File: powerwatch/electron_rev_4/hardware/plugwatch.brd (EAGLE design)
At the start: 55.7 x 95.2 mm, 128 parts, among them J1 CON_MICRO_SDDM3AT-SF-PEJM5, U1 BGA725L6-ALT, U10 SIP32510, U12 SIP32510, U13 AB1815-T3, U16 MAX6746, U2 SAFFB1G56KB0F0A, U20 DS2401P+, U3 IRM-03-5V, U4 MAX-M8, U5 OPA369, U6 LIS2DW12, U8 OPA369, U9 SIP32510, X1 ABS07-32.768KHZ-7-T

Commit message: renumbered eagle parts
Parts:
- removed C19: 0.1uF, passives:0402_CAP
- removed C26: 4.7uF, passives:0402_CAP
- removed D11: (no value), passives:SOD323
- removed J4: (no value), SparkFun-Connectors:JST-2-SMD
- removed RF, RF1: 4.99k 1%, passives:0402_RES
- removed RI1, RI3: 953k 1%, passives:1206_RES_HIGH_CLEARANCE
- removed RI2, RI4: 953k 1%, passives:0402_RES
- removed U16: MAX6746, chips:SOT-23-8
- removed U20: DS2401P+, DS2401P+:21-0382
- added C10: 1uF, passives:0402_CAP
- added C16: 100uF, passives:1210_CAP
- added D2: (no value), passives:SOD323
- added J2: (no value), SparkFun-Connectors:JST-2-SMD
- added R20: 34k, passives:0402_RES
- added R37, R38, R39, R40: 1M, passives:0402_RES
- added U11: SIP32510, chips:TSOT23-6
- added U14: (no value), microphones:SPH0465
- added V1: S14K385, varistor:S14K385
- C1: value 1uF -> 47pF
- C11: value 10nF -> 1uF
- C12: value 10nF -> 4.7uF
- C15: value 100nF -> 100uF; device passives:0402_CAP -> passives:1210_CAP
- C17: value 100uF -> 2000uF; device passives:1210_CAP -> rcl:E5-13
- C2: value 2000uF -> 10nF; device rcl:E5-13 -> passives:0402_CAP
- C3: value 47pF -> 10nF
- C4: value 1uF -> 0.1uF
- C7: value 100uF -> 100nF; device passives:1210_CAP -> passives:0402_CAP
- D1: value BLUE -> (none); device leds:LED-0603 -> passives:SOD323
- D4, D5, D6, D7: value 3.3V -> (none)
- D9: value (none) -> BLUE; device passives:SOD323 -> leds:LED-0603
- R1: value 10k -> 66.5
- R10: value 10k -> 5k
- R11: value 68 -> 10k
- R15, R16, R17, R18, R19: value 100k -> 10k
- R2: value 10k -> 68
- R21: value 750k -> 100k; device passives:1206_RES_HIGH_CLEARANCE -> passives:0402_RES
- R22, R23, R25: value 1M 1% -> 100k
- R24: value 835k -> 100k
- R26: value 68 -> 100k
- R28: value 1M 1% -> 750k; device passives:0402_RES -> passives:1206_RES_HIGH_CLEARANCE
- R29: value 5K -> 750k; device passives:0402_RES -> passives:1206_RES_HIGH_CLEARANCE
- R32: value 1.5k -> 835k
- R33: value 1.5k -> 953k
- R34: value 10k -> 953k
- R35: value 66.5 -> 953k; device passives:0402_RES -> passives:1206_RES_HIGH_CLEARANCE
- R36: value 34k -> 953k; device passives:0402_RES -> passives:1206_RES_HIGH_CLEARANCE
- R4: value 1k -> 68
- R5: value 100k -> 1k
- R6: value 10k -> 1.5k
- R7: value S14K385 -> 1.5k; device varistor:S14K385 -> passives:0402_RES
- R8: value 750k -> 4.99k; device passives:1206_RES_HIGH_CLEARANCE -> passives:0402_RES
- R9: value 10k -> 4.99k
- U1: value BGA725L6-ALT -> AB1815-T3; device Particle:LNA-TSLP-6-2-ALT -> chips:QFN-16-3MM
- U10, U9: value SIP32510 -> OPA369; device chips:TSOT23-6 -> powerfilm:SC70-5
- U13: value AB1815-T3 -> SIP32510; device chips:QFN-16-3MM -> chips:TSOT23-6
- U2: value SAFFB1G56KB0F0A -> BGA725L6-ALT; device Particle:QCS5I -> Particle:LNA-TSLP-6-2-ALT
- U3: value IRM-03-5V -> DS2401P+; device powerwatch:IRM-03 -> DS2401P+:21-0382
- U4: value MAX-M8 -> SAFFB1G56KB0F0A; device u-blox:MAX-M8 -> Particle:QCS5I
- U5: value OPA369 -> IRM-03-5V; device powerfilm:SC70-5 -> powerwatch:IRM-03
- U7: value (none) -> MAX-M8; device microphones:SPH0465 -> u-blox:MAX-M8
- U8: value OPA369 -> MAX6746; device powerfilm:SC70-5 -> chips:SOT-23-8
- moved R36 71.4 mm to (6.86, 15.4)
- moved U3 70.2 mm to (3.05, 80.5), turned to 270 degrees
- moved R25 66.2 mm to (7.37, 76.2), turned to 180 degrees
- moved R29 64.8 mm to (6.86, 19.9), turned to 180 degrees
- moved R34 62.0 mm to (2.79, 14.2)
- moved U8 59.2 mm to (32.6, 63.2), turned to 90 degrees
- moved R9 59.1 mm to (2.79, 13.3), turned to 180 degrees
- moved R35 57.2 mm to (6.99, 29.7)
- moved R21 56.3 mm to (31.2, 70.7), turned to 90 degrees
- moved U10 56.2 mm to (3.17, 11.9), turned to 180 degrees
- moved U9 55.5 mm to (3.43, 33.0), turned to 90 degrees
- moved R22 52.2 mm to (28.4, 76.8), turned to 0 degrees
- moved U13 44.1 mm to (49.8, 63.6), turned to 0 degrees
- moved R23 44.0 mm to (39.9, 55.8)
- moved D9 44.0 mm to (37.3, 50.0), turned to 90 degrees
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- renumbered A2 to A1, B2 to B1, C100 to C5, C101 to C6, C24 to C9, C27 to C14, C29 to C8, D10 to D3, L4 to L2, L5 to L3
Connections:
- net !EXTERNAL_RST: now also R19.2, TP26.TESTPOINT, U8.7; no longer R1.2, TP17.TESTPOINT, U16.7
- net !GPS_RESET: now also TP10.TESTPOINT, U7.9; no longer TP23.TESTPOINT, U4.9
- net !RTC_CS: now also R18.2, TP23.TESTPOINT, U1.12; no longer R6.2, TP11.TESTPOINT, U13.12
- net !RTC_INT1: now also R17.2, TP24.TESTPOINT, U1.11; no longer R34.2, TP15.TESTPOINT, U13.11
- net !SD_CS: now also TP18.TESTPOINT; no longer TP6.TESTPOINT
- net !SD_DETECT: now also R21.1, TP11.TESTPOINT; no longer R16.1, TP24.TESTPOINT
- net 5V: now also C15.1, C16.1, C17.+, R20.1, R25.1, U5.V+; no longer C17.1, C2.+, C7.1, R36.1, R5.1, U3.V+
- net AC/L-FUSED: now also R28.1, R35.1, U5.AC/L, V1.1; no longer R7.1, R8.1, RI1.1, U3.AC/L
- net AC/L-MEASURE: now also D1.P$1, D5.P$1; no longer D6.P$1, D8.P$1
- net AC/L-PERTURB: now also D2.P$1, D6.P$1, R28.2, TP27.TESTPOINT; no longer D4.P$1, D9.P$1, R8.2, TP25.TESTPOINT
- net AC/L-SENSE: now also R8.2, U9.P4; no longer RF.2, U5.P4
- net AC/N-FUSED: now also R29.1, R36.1, U5.AC/N, V1.2; no longer R21.1, R7.2, RI3.1, U3.AC/N
- net AC/N-MEASURE: now also D7.P$1, TP28.TESTPOINT; no longer D5.P$1, TP27.TESTPOINT
- net AC/N-PERTURB: now also D4.P$1, D8.P$1, R29.2; no longer D11.P$1, D7.P$1, R21.2
- net AC/N-SENSE: now also R9.2, U10.P4; no longer RF1.2, U8.P4
- net ACCEL_INT: now also TP8.TESTPOINT; no longer TP21.TESTPOINT
- net GND: now also C10.2, C11.2, C12.2, C15.2, C16.2, C17.-, C2.1, C3.1, C7.1, D1.P$2, D2.P$2, J2.1, R1.2, R16.2, R22.1, R24.1, R26.2, R33.1, R34.1, R38.1, R40.1, TP12.TESTPOINT, U1.3, U1.GND, U10.P2, U11.4, U13.4, U14.3, U2.1, U2.4, U3.1, U4.2, U4.3, U4.5, U5.V-, U7.1, U7.10, U7.12, U8.4, U9.P2; no longer C11.1, C12.1, C15.1, C17.2, C19.2, C2.-, C26.2, C3.2, C7.2, D11.P$2, D9.P$2, J4.1, R15.2, R17.1, R18.1, R19.1, R2.2, R28.1, R35.2, RI2.1, RI4.1, TP26.TESTPOINT, U1.1, U1.4, U10.4, U13.3, U13.GND, U16.4, U2.2, U2.3, U2.5, U20.1, U3.V-, U4.1, U4.10, U4.12, U5.P2, U7.3, U8.P2, U9.4
- net GPS_PWR_EN: now also R23.2, TP9.TESTPOINT, U11.3; no longer R18.2, TP22.TESTPOINT, U10.3
- net GPS_RF_IN: now also U4.4, U7.11; no longer U2.4, U4.11
- net GPS_RXD: now also TP6.TESTPOINT; no longer TP1.TESTPOINT
- net GPS_TXD: now also TP14.TESTPOINT; no longer TP2.TESTPOINT
- net GPS_VCC: now also C3.2, C7.2, R5.2, U11.1, U11.2, U7.6, U7.7, U7.8; no longer C12.2, C15.2, R4.2, U10.1, U10.2, U4.6, U4.7, U4.8
- net LNA_IN: now also U2.5; no longer U1.5
- net LNA_OUT: now also U2.3, U4.1; no longer U1.3, U2.1
- net MIC_BCLK: now also R3.2, TP22.TESTPOINT; no longer R11.2, TP10.TESTPOINT
- net MIC_DATA: now also R4.1, TP21.TESTPOINT; no longer R26.1, TP9.TESTPOINT
- net MIC_WS: now also R2.2, TP20.TESTPOINT; no longer R3.2, TP8.TESTPOINT
- net N$1: now also D9.A, R5.1; no longer D1.A, R4.1
- net N$10: now also R1.1, R20.2; no longer R35.1, R36.2
- net N$12: now also R3.1, U14.4; no longer R11.1, U7.4
- net N$13: now also C1.1, U1.14; no longer C3.1, U13.14
- net N$14: now also U13.1, U13.2; no longer U9.1, U9.2
- net N$15: now also R4.2, U14.6; no longer R26.2, U7.6
- net N$18: now also C12.1, R21.2; no longer C26.1, R16.2
- net N$2: now also D9.C, U7.4; no longer D1.C, U4.4
- net N$20: now also U1.15; no longer U13.15
- net N$21: now also U1.16; no longer U13.16
- net N$23: now also J2.2, R19.1, R32.1, U8.5, U8.8; no longer J4.2, R1.1, R24.1, U16.5, U16.8
- net N$25: now also R25.2, R26.1, U1.10; no longer R15.1, R5.2, U13.10
- net N$3: now also R2.1, U14.1; no longer R3.1, U7.1
- net N$31: now also R32.2, U8.1; no longer R24.2, U16.1
- net N$36: now also U8.3; no longer U16.3
- net N$39: now also U8.2; no longer U16.2
- net N$4: now also R6.2, R7.1; no longer R32.2, R33.1
- net N$40: now also U7.2; no longer U4.2
- net N$41: now also U7.3; no longer U4.3
- net N$42: now also R37.1, R38.2, U9.P1; no longer R22.1, R23.2, U5.P1
- net N$43: now also R33.2, R35.2, R8.1, U9.P3; no longer RF.1, RI1.2, RI2.2, U5.P3
- net N$44: now also R39.1, R40.2, U10.P1; no longer R25.1, R28.2, U8.P1
- net N$45: now also R34.2, R36.2, R9.1, U10.P3; no longer RF1.1, RI3.2, RI4.2, U8.P3
- net N$5: now also R7.2, U1.5; no longer R33.2, U13.5
- net SD_ENABLE: now also R22.2, TP19.TESTPOINT; no longer R17.2, TP7.TESTPOINT
- net SD_MISO: now also TP16.TESTPOINT, U1.6; no longer TP4.TESTPOINT, U13.6
- net SD_MOSI: now also TP15.TESTPOINT, U1.9; no longer TP3.TESTPOINT, U13.9
- net SD_SCLK: now also TP17.TESTPOINT, U1.7; no longer TP5.TESTPOINT, U13.7
- net SENSORS_SCL: now also R15.1, TP7.TESTPOINT; no longer R9.1, TP20.TESTPOINT
- net SENSORS_SDA: now also R11.1, TP5.TESTPOINT; no longer R10.1, TP19.TESTPOINT
- net SERIAL_NUM: now also R10.2, TP13.TESTPOINT, U3.2; no longer R29.2, TP28.TESTPOINT, U20.2
- net VCC: now also C10.1, C11.1, R10.1, R11.2, R15.2, R17.1, R18.1, R37.2, R39.2, TP4.TESTPOINT, U1.13, U10.P5, U11.5, U11.6, U13.5, U13.6, U14.2, U14.5, U9.P5; no longer C1.1, C19.1, R10.2, R22.2, R25.2, R29.1, R32.1, R34.1, R9.2, TP18.TESTPOINT, U10.5, U10.6, U13.13, U5.P5, U7.2, U7.5, U8.P5, U9.5, U9.6
- net VCC_RF: now also C2.2, U2.2, U2.6, U7.14; no longer C11.2, U1.2, U1.6, U4.14
- net WDI: now also R16.1, TP25.TESTPOINT, U1.2, U8.6; no longer R2.1, TP16.TESTPOINT, U13.2, U16.6
- net WIFI_PWR_EN: now also R24.2, TP1.TESTPOINT, U13.3; no longer R19.2, TP12.TESTPOINT, U9.3
- net WIFI_RXD: now also TP3.TESTPOINT; no longer TP14.TESTPOINT
- net WIFI_TXD: now also TP2.TESTPOINT; no longer TP13.TESTPOINT

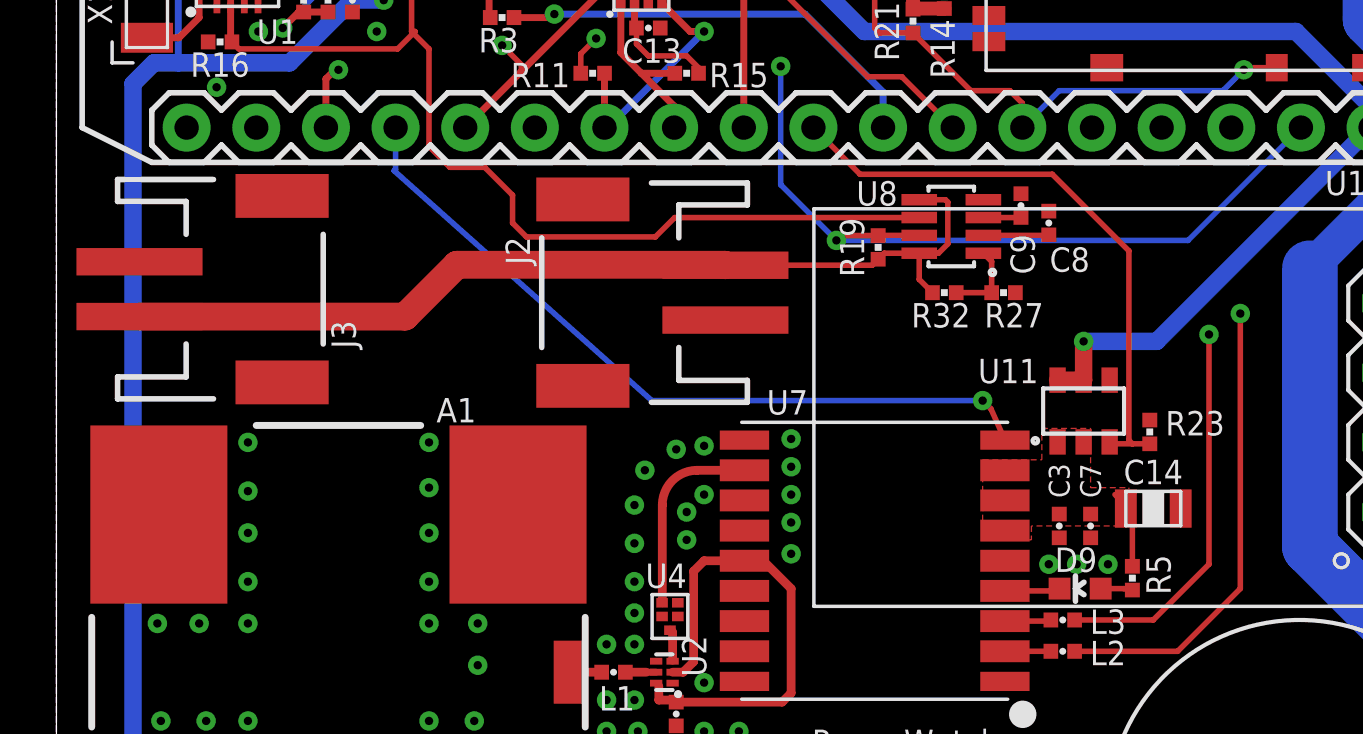
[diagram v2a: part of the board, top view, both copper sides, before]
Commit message: fixed up BOM and attributes
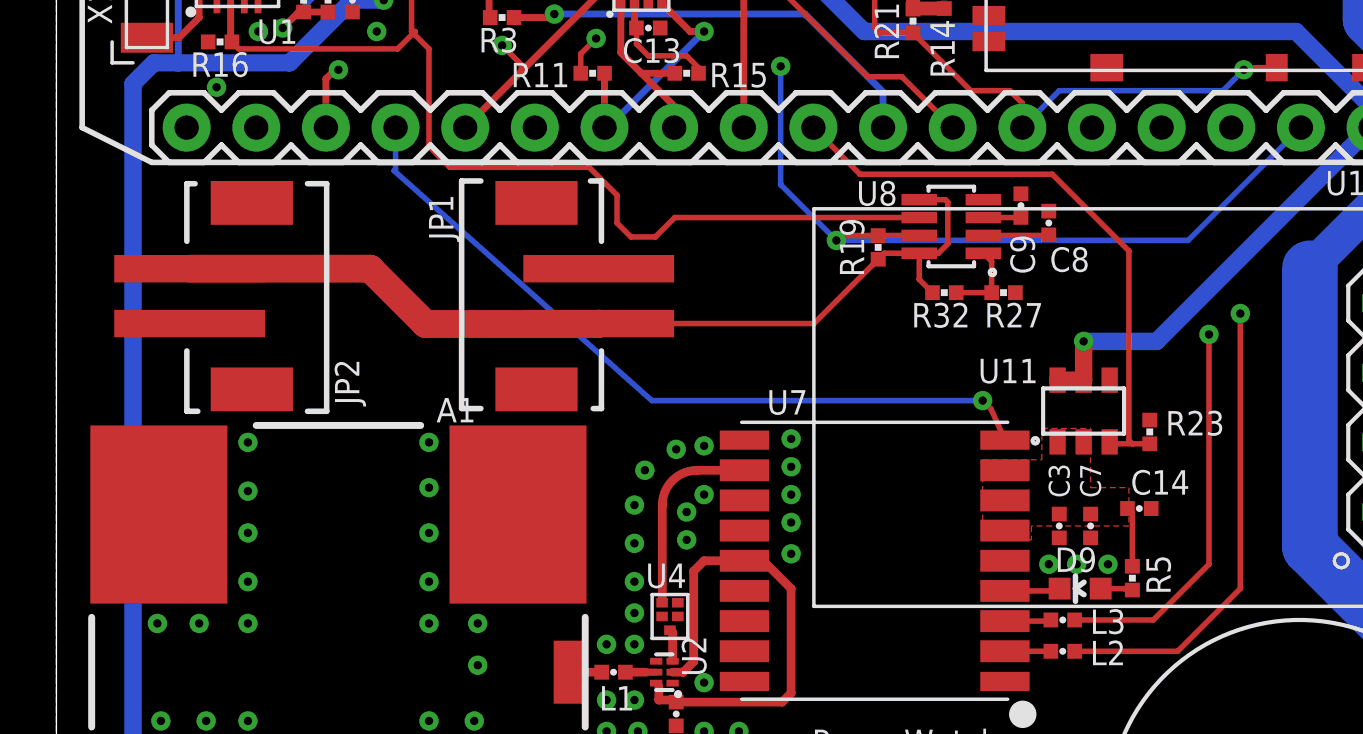
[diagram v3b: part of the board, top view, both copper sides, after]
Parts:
- removed J2, J3: (no value), SparkFun-Connectors:JST-2-SMD
- added JP1, JP2: (no value), SparkFun-Connectors:JST-2-SMD-VERT
- C14: device passives:0805_CAP -> passives:0402_CAP
- C7: value 100nF -> 0.1uF
- C8: value 0.47uF -> 2.2uF
- J1: value CON_MICRO_SDDM3AT-SF-PEJM5 -> DM3AT-SF-PEJM5
- R10: value 5k -> 5.1k
- R27: value 500k -> 499k
- R32: value 835k -> 825k
- U8: value MAX6746 -> MAX67XXMAX6749MAX67XX
- moved C14 0.51 mm to (39.5, 53.0), turned to 180 degrees
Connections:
- net GND: now also C14.1, JP1.GND, JP2.GND; no longer C14.P$1, J2.1, J3.1
- net GPS_VCC: now also C14.2; no longer C14.P$2
- net N$23: now also JP1.VCC, JP2.VCC; no longer J2.2, J3.2
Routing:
- net GPS_VCC: track 3.32 -> 2.18 mm
- net N$23: track 34.8 -> 34.2 mm
